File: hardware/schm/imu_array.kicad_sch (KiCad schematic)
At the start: 16 parts, among them U3 MCP23S17T-E/SS, U4 LSM6DSV320XTR, U5 H3LIS331DLTR, U6 H3LIS331DLTR

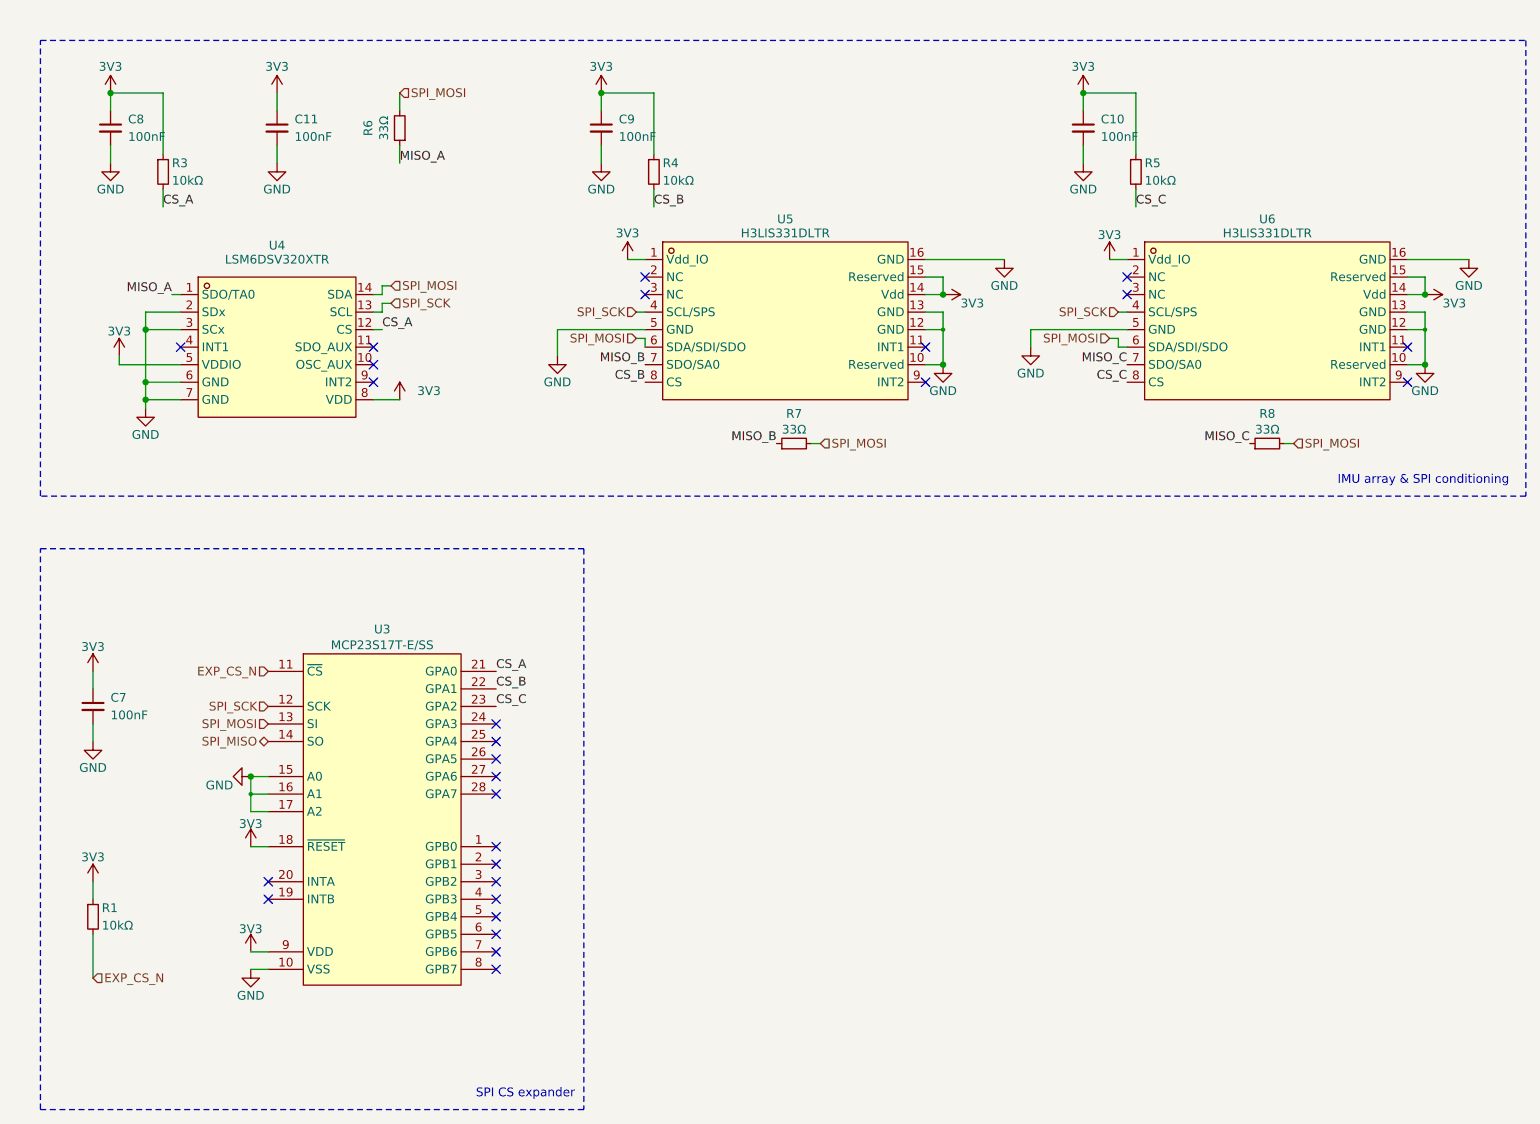
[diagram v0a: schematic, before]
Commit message: feat: organize subsheets
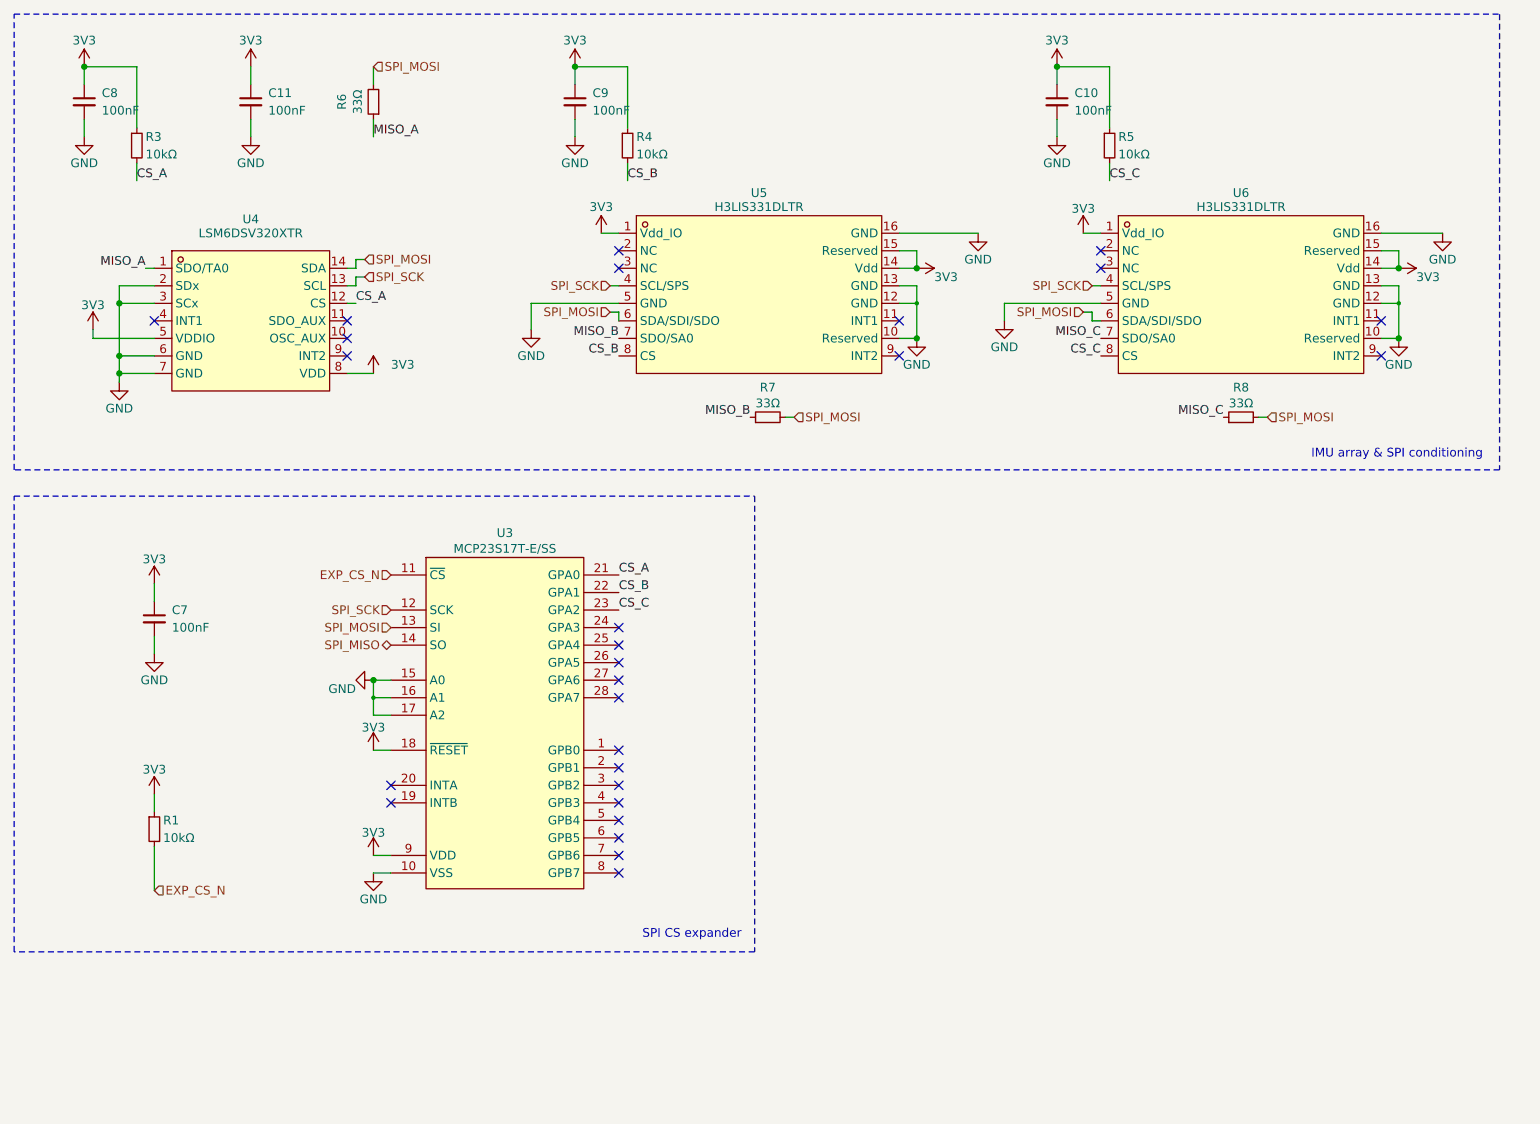
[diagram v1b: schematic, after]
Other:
- company: (none) -> Kieran Klukas
- title: (none) -> Holy Guacamole
- moved on the sheet: C10, C11, C7, C8, C9, R1, R3, R4, R5, R6, R7, R8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

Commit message: feat: organize into better sheets
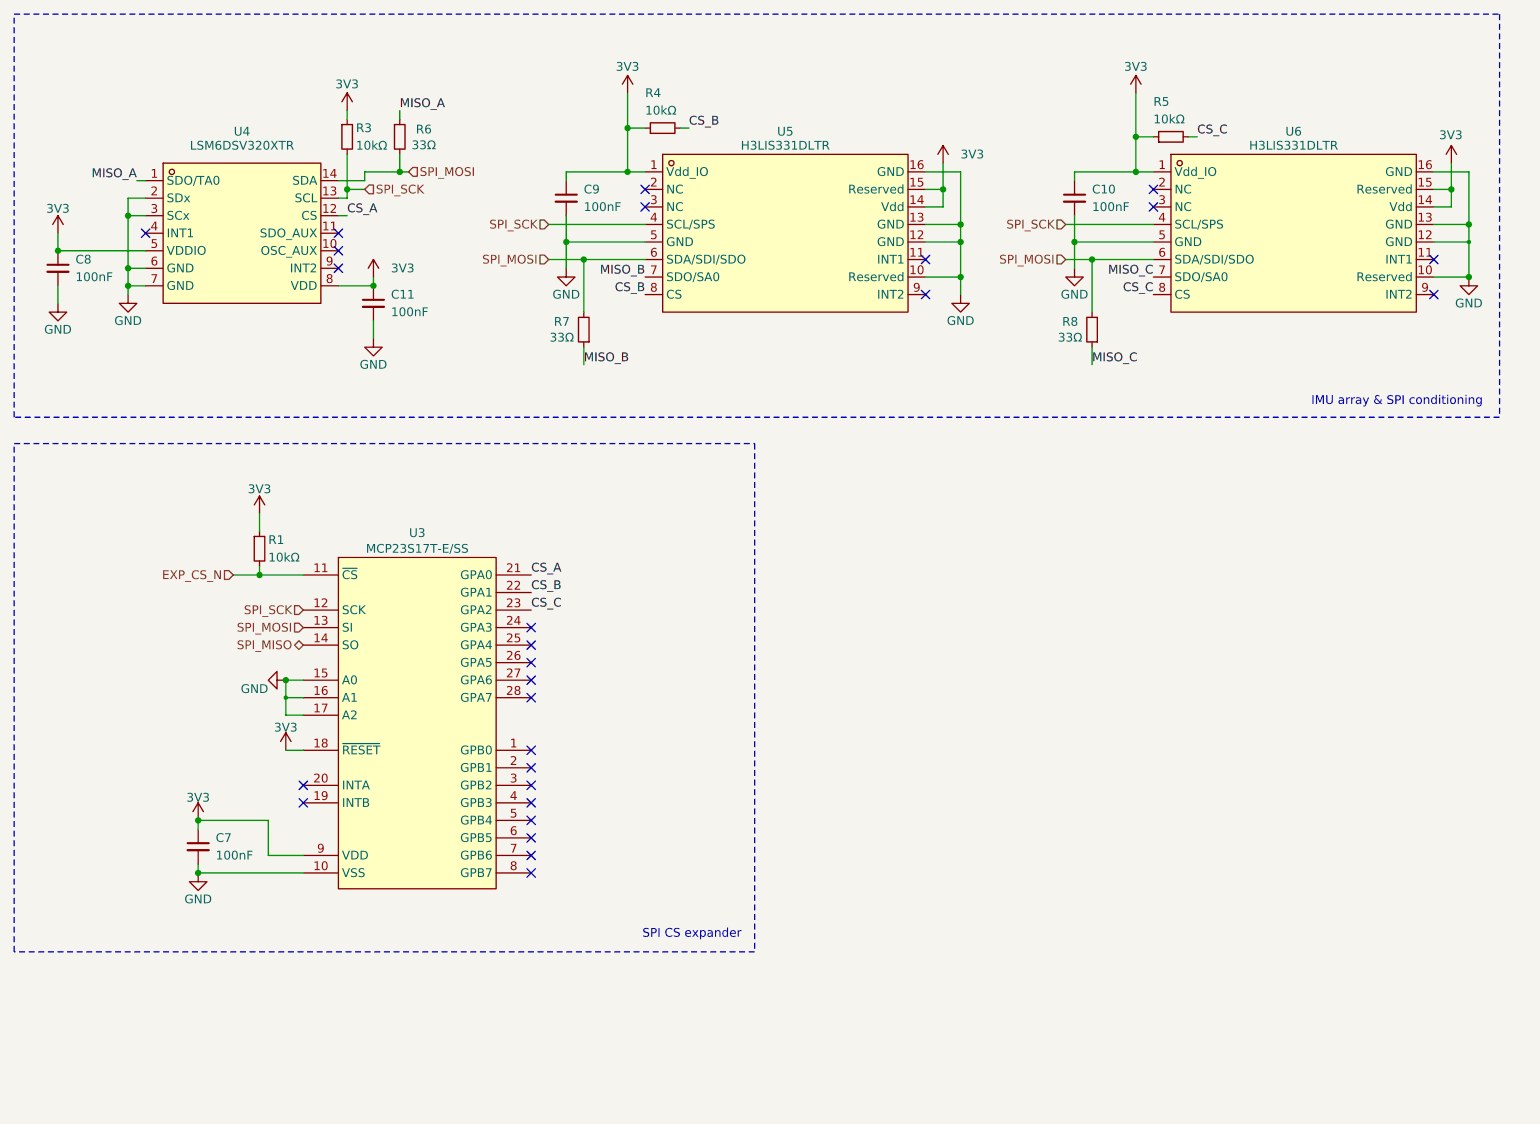
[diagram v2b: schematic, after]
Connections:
- net CS_A: no longer R3.2
- net SPI_SCK: now also R3.2
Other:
- moved on the sheet: C7, R1, R6, R7, R8, U3, U4, U5, U6
